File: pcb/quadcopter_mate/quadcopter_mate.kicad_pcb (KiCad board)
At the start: 2 copper layers, 48.3 x 73.7 mm, 8 parts, among them J1 RJ45

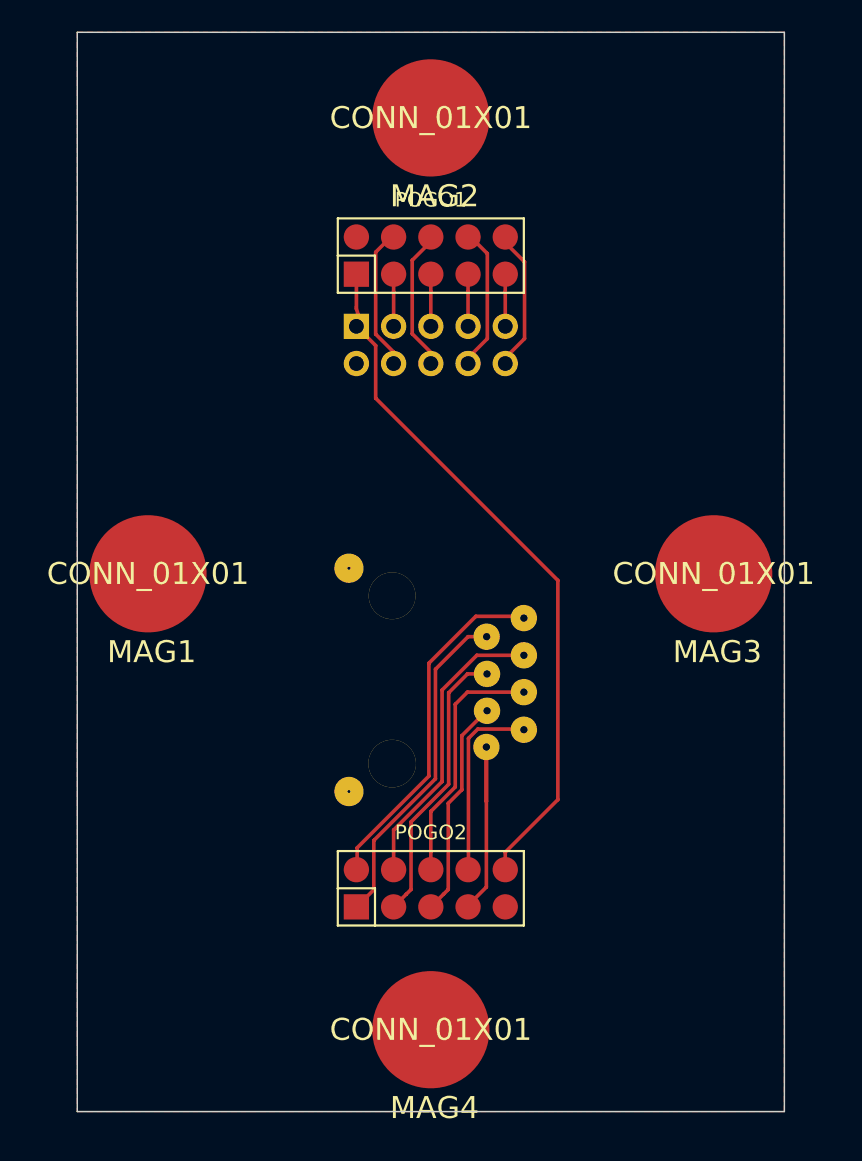
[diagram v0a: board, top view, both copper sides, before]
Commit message: Added cal poly logo and set up backside
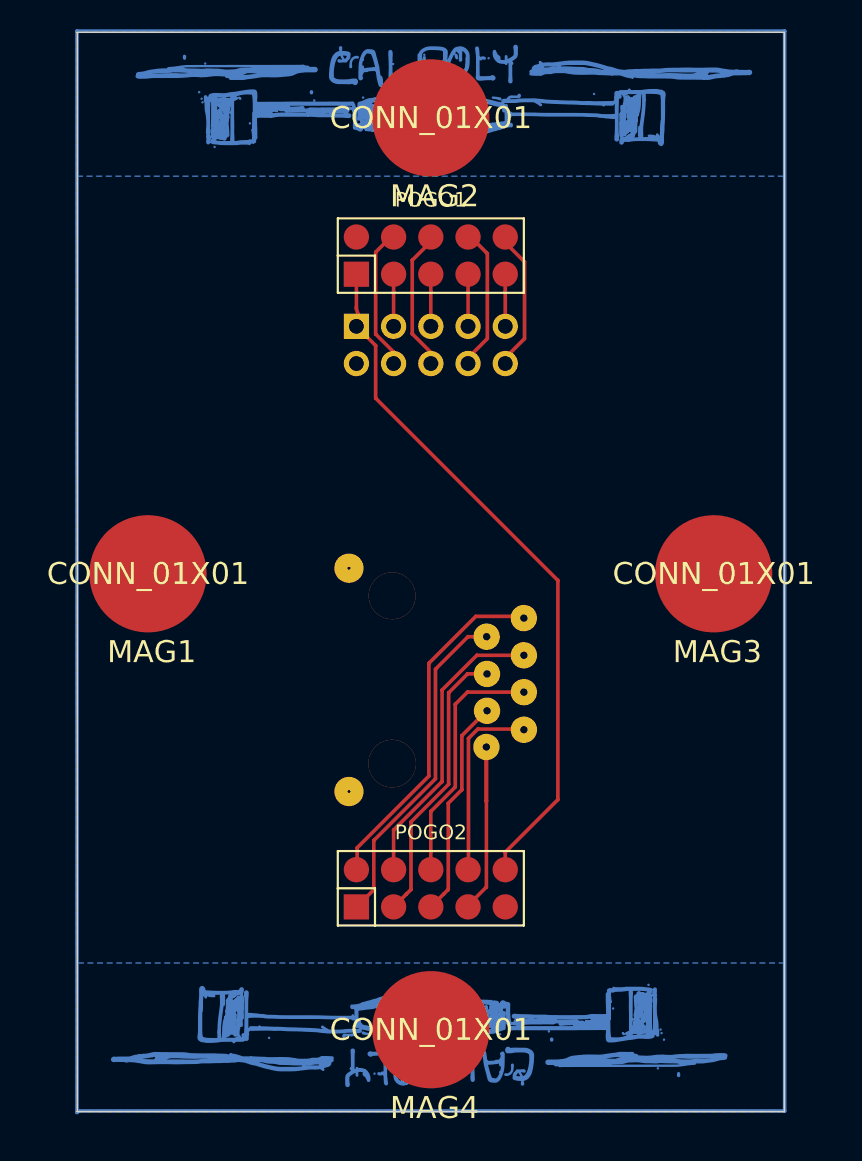
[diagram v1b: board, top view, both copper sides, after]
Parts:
- added G***: LOGO, quadcopter_footprints:logo, F.Cu at (228.9, 62.0)
- added G***: LOGO, quadcopter_footprints:logo, F.Cu at (227.5, 124.2)
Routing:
- net (no net): track 0.00 -> 244.1 mm
- added copper zone on B.Cu, net GND
